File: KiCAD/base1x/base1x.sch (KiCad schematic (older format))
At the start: 83 parts, among them J1 Conn_02x05_Odd_Even, J10 Conn_01x03, J11 Conn_01x03, J12 Conn_01x03, J13 Conn_01x03, J14 Conn_01x03, J15 Conn_01x08, J17 Conn_01x03, J18 Conn_01x03, J19 Conn_01x03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

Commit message: base1x doneish
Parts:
- removed R10, R9: 50R, Resistor_SMD:R_1206_3216Metric, symbol Device:R_Small
- removed R7: 900k, Resistor_SMD:R_1206_3216Metric, symbol Device:R_Small
- removed R8: 100k, Resistor_SMD:R_1206_3216Metric, symbol Device:R_Small
- removed U6, U7: AD8615, Package_TO_SOT_SMD:TSOT-23-5, symbol Amplifier_Operational:AD8603
- added C14, C15, C16, C17, C18: 0.1uF, Capacitor_SMD:C_1206_3216Metric, symbol Device:C_Small
- added J16: Conn_02x05_Odd_Even, Connector_IDC:IDC-Header_2x05_P2.54mm_Vertical, symbol Connector_Generic:Conn_02x05_Odd_Even
- added J20: Conn_01x03, Connector_PinHeader_1.27mm:PinHeader_1x03_P1.27mm_Vertical, symbol Connector_Generic:Conn_01x03
- added JP4: Jumper_NO_Small, Jumper:SolderJumper-2_P1.3mm_Open_RoundedPad1.0x1.5mm, symbol Device:Jumper_NO_Small
- added R4: 51R, Resistor_SMD:R_1206_3216Metric_Pad1.42x1.75mm_HandSolder, symbol Device:R_Small
- added U1: AD8616, Package_SO:SOIC-8_3.9x4.9mm_P1.27mm, symbol Amplifier_Operational:AD8620
- C1, C2, C3, C5, C6, C8: farnell code (none) -> 1759297
- C10, C9: farnell code (none) -> 1759453
- C11, C4, C7: value 1000pF -> 0.1uF; farnell code 1855909 -> 1759297
- C12, C13: footprint (none) -> Capacitor_Tantalum_SMD:CP_EIA-7343-43_Kemet-X_Pad2.25x2.55mm_HandSolder
- D1, D2: I_max 20mA -> 2mA
- D10, D3, D4, D5, D6, D7, D8, D9: farnellCode (none) -> 9843760
- J1: footprint Connector_IDC:IDC-Header_2x05_P2.54mm_Horizontal -> Connector_IDC:IDC-Header_2x05_P2.54mm_Vertical; farnellCode 2215290 -> 2215304
- J10, J11, J12, J13, J14, J17, J18, J19, J2, J4, J5: footprint (none) -> Connector_PinHeader_1.27mm:PinHeader_1x03_P1.27mm_Vertical; farnell code (none) -> 2578712+2505013
- J15: footprint (none) -> Converter_DCDC:Converter_DCDC_TRACO_TMR-xxxx_THT; Farnell Code (none) -> 495-TMR6-0521
- J3: farnell code (none) -> 1097986
- J6: value Conn_02x14_Counter_Clockwise -> Conn_01x14_Counter_Clockwise; footprint Connector_PinSocket_2.54mm:PinSocket_2x14_P2.54mm_Vertical -> Connector_PinHeader_2.54mm:PinHeader_1x14_P2.54mm_Vertical; farnellCode (none) -> 1593466
- JP3: footprint (none) -> Jumper:SolderJumper-2_P1.3mm_Open_RoundedPad1.0x1.5mm
- R1: footprint Resistor_SMD:R_1206_3216Metric -> Resistor_SMD:R_2010_5025Metric_Pad1.52x2.65mm_HandSolder; farnellCode 2073607 -> 1887405
- R11: value 50R -> 51R; footprint Resistor_SMD:R_1206_3216Metric -> Resistor_SMD:R_1206_3216Metric_Pad1.42x1.75mm_HandSolder; farnellCode 2476379 -> 2695165
- R2, R3: value 100R -> 1k; footprint Resistor_SMD:R_1206_3216Metric -> Resistor_SMD:R_1206_3216Metric_Pad1.42x1.75mm_HandSolder; farnellCode 2476379 -> 2447473
- R5: value 900k -> 51R; footprint Resistor_SMD:R_1206_3216Metric -> Resistor_SMD:R_1206_3216Metric_Pad1.42x1.75mm_HandSolder; farnellCode 2476379 -> 2695165
- R6: value 100k -> 1k; footprint Resistor_SMD:R_1206_3216Metric -> Resistor_SMD:R_1206_3216Metric_Pad1.42x1.75mm_HandSolder; farnellCode 2476379 -> 2447473
- U2, U5: footprint (none) -> Package_SO:TSSOP-16_4.4x5mm_P0.65mm; Farnell Code (none) -> 296-50885-1-ND
- U8: value LT1963AxQ-2.5 -> LT1963EQ-2.5; Farnell Code (none) -> LT1963EQ-2.5#PBF-ND
- U9: value LT3015xQ-2.5 -> LT3015EQ-2.5; Farnell Code (none) -> 584-LT3015EQ-2.5#PBF
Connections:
- net +2V5: now also C4.2, C8.1, C16.1, U1.8 (V+); no longer C5.1, R5.2
- net +5V: now also C7.1, C14.1, J16.2 (Pin_2); no longer C3.1, C8.1
- net -2V5: now also C11.1, C5.2, C17.1, U1.4 (V-); no longer C6.1
- net EnableTraco: now also J16.5 (Pin_5)
- net GND: now also C7.2, C14.2, J16.6 (Pin_6); no longer C3.2, C8.2
- net GNDREF: now also C11.2, C4.1, C5.1, C8.2, C16.2, C17.2, U1.3 (+), U1.5 (+); no longer C5.2, C6.2, R6.1
- net MISO: now also J16.1 (Pin_1)
- net MOSI: now also J16.4 (Pin_4)
- net SCK: now also J16.3 (Pin_3)
- net SCL: now also J16.8 (Pin_8)
- net SDA: now also J16.7 (Pin_7)
- net V_Current: now also R11.2, U2.10 (AIN1); no longer C4.2, R1.1, R11.1, TP2.1, U3.1
- net V_D1: now also R5.2
- net V_D2: now also R4.2
- net Vin: now also JP4.1
- net ~CS0: now also J16.10 (Pin_10)
- net at D1.1 (K), R3.2: now also C18.1, U1.2 (-); no longer C11.1
- net at D2.1 (K), R2.2: now also C15.1, U1.6 (-); no longer C7.1
- net at R2.1, TP4.1: now also C15.2, R4.1, U1.7; no longer C7.2
- net at R5.1: now also R3.1, TP3.1, C18.2, U1.1; no longer R6.2
- net at J4.3 (Pin_3), R1.2, U3.4 (-): now also C3.2, C6.2, R6.1; no longer C4.1
- new net: J16.9 (Pin_9), JP4.2
- new net: J20.2 (Pin_2), R11.1, TP2.1, U3.1
- new net: C3.1, J20.1 (Pin_1), R1.1
- new net: C6.1, J20.3 (Pin_3), R6.2
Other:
- note added: "1 Sun -> ~~1mA through the PD -> ~~1V to the ADC"
- note added: "COMM_BUS_MIRROR"
- note added: "Consider switching to LT1997-1 (this TIA limits current to 150mA)"
- note added: "Gain=20V/A\nor 1000V/A\n(dark mode)"
- note removed: "Bias Voltage"
- note removed: "Current Sense TIA"
- note removed: "Gain=20V/A"
- moved on the sheet: D10, D2, D3, D4, D5, D6, D7, D8, D9, J13, J14, J17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

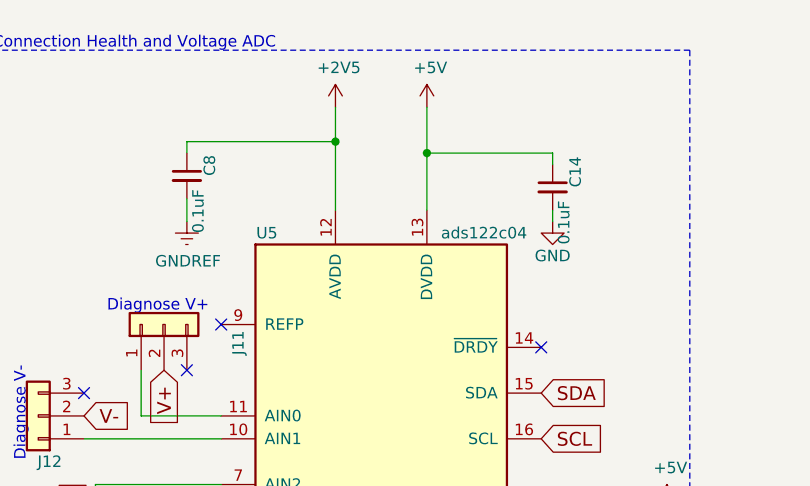
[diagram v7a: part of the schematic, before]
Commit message: new base1x layed out, mux updated and re-layed out
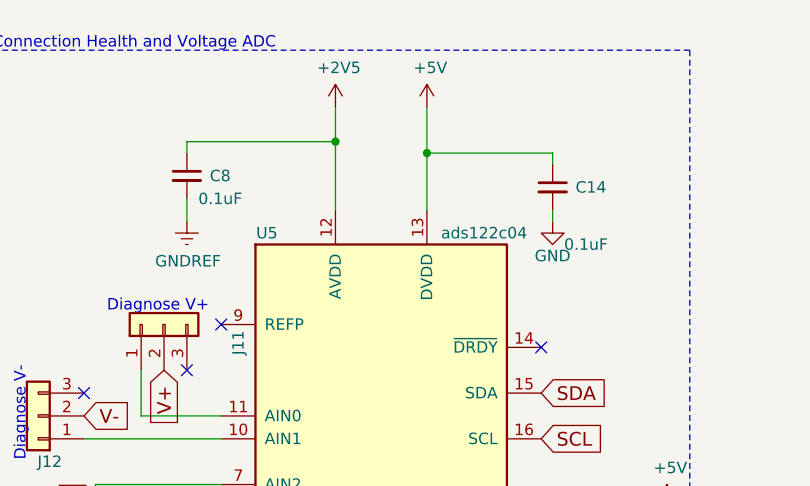
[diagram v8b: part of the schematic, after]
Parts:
- C1, C10, C11, C14, C15, C16, C17, C18, C2, C3, C4, C5, C6, C7, C8, C9: footprint Capacitor_SMD:C_1206_3216Metric -> Capacitor_SMD:C_1206_3216Metric_Pad1.42x1.75mm_HandSolder
- J6: footprint Connector_PinHeader_2.54mm:PinHeader_1x14_P2.54mm_Vertical -> Connector_PinSocket_2.54mm:PinSocket_1x14_P2.54mm_Vertical
- L1: footprint logo:logo_and_text -> logo:text
- R1: footprint Resistor_SMD:R_2010_5025Metric_Pad1.52x2.65mm_HandSolder -> Resistor_SMD:R_1206_3216Metric_Pad1.42x1.75mm_HandSolder
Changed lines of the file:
@@
 F 0 "L1" H 9050 6675 60  0001 C CNN
 F 1 "grey@mutovis.com" H 9000 6550 100 0000 C CNN
-F 2 "logo:logo_and_text" H 9050 6800 60  0001 C CNN
+F 2 "logo:text" H 9050 6800 60  0001 C CNN
 F 3 "" H 9050 6800 60  0001 C CNN
 	1    9050 6800
@@
 F 0 "J6" H 10950 6350 50  0000 C CNN
 F 1 "Conn_01x14_Counter_Clockwise" H 10950 6376 50  0001 C CNN
-F 2 "Connector_PinHeader_2.54mm:PinHeader_1x14_P2.54mm_Vertical" H 10900 5650 50  0001 C CNN
+F 2 "Connector_PinSocket_2.54mm:PinSocket_1x14_P2.54mm_Vertical" H 10900 5650 50  0001 C CNN
 F 3 "" H 10900 5650 50  0001 C CNN
 F 4 "1593466" H 0   0   50  0001 C CNN "farnellCode"
@@
 F 0 "C9" H 7292 1596 50  0000 L CNN
 F 1 "10uF" H 7292 1505 50  0000 L CNN
-F 2 "Capacitor_SMD:C_1206_3216Metric" H 7200 1550 50  0001 C CNN
+F 2 "Capacitor_SMD:C_1206_3216Metric_Pad1.42x1.75mm_HandSolder" H 7200 1550 50  0001 C CNN
 F 3 "" H 7200 1550 50  0001 C CNN
 F 4 "1759453" H 0   0   50  0001 C CNN "farnell code"
@@
 F 0 "C10" H 7292 2846 50  0000 L CNN
 F 1 "10uF" H 7292 2755 50  0000 L CNN
-F 2 "Capacitor_SMD:C_1206_3216Metric" H 7200 2800 50  0001 C CNN
+F 2 "Capacitor_SMD:C_1206_3216Metric_Pad1.42x1.75mm_HandSolder" H 7200 2800 50  0001 C CNN
 F 3 "" H 7200 2800 50  0001 C CNN
 F 4 "1759453" H 0   0   50  0001 C CNN "farnell code"
@@
 F 0 "R1" V 1950 4300 50  0000 C CNN
 F 1 "20R" V 2155 4300 50  0000 C CNN
-F 2 "Resistor_SMD:R_2010_5025Metric_Pad1.52x2.65mm_HandSolder" H 2050 4300 50  0001 C CNN
+F 2 "Resistor_SMD:R_1206_3216Metric_Pad1.42x1.75mm_HandSolder" H 2050 4300 50  0001 C CNN
 F 3 "" H 2050 4300 50  0001 C CNN
 F 4 "1887405" H -4950 1950 50  0001 C CNN "farnellCode"
@@
 F 0 "C15" V 7150 4950 50  0000 L CNN
 F 1 "0.1uF" V 7100 4700 50  0000 L CNN
-F 2 "Capacitor_SMD:C_1206_3216Metric" H 7050 4950 50  0001 C CNN
+F 2 "Capacitor_SMD:C_1206_3216Metric_Pad1.42x1.75mm_HandSolder" H 7050 4950 50  0001 C CNN
 F 3 "" H 7050 4950 50  0001 C CNN
 F 4 "1759297" V 7050 4950 50  0001 C CNN "farnell code"
@@
 F 0 "C18" V 9700 4900 50  0000 L CNN
 F 1 "0.1uF" V 9650 4650 50  0000 L CNN
-F 2 "Capacitor_SMD:C_1206_3216Metric" H 9600 4900 50  0001 C CNN
+F 2 "Capacitor_SMD:C_1206_3216Metric_Pad1.42x1.75mm_HandSolder" H 9600 4900 50  0001 C CNN
 F 3 "" H 9600 4900 50  0001 C CNN
 F 4 "1759297" V 9600 4900 50  0001 C CNN "farnell code"
@@
 F 0 "C16" V 8600 5100 50  0000 L CNN
 F 1 "0.1uF" V 8550 4850 50  0000 L CNN
-F 2 "Capacitor_SMD:C_1206_3216Metric" H 8500 5100 50  0001 C CNN
+F 2 "Capacitor_SMD:C_1206_3216Metric_Pad1.42x1.75mm_HandSolder" H 8500 5100 50  0001 C CNN
 F 3 "" H 8500 5100 50  0001 C CNN
 F 4 "1759297" V 8500 5100 50  0001 C CNN "farnell code"
@@
 F 0 "C17" V 8600 5800 50  0000 L CNN
 F 1 "0.1uF" V 8550 5550 50  0000 L CNN
-F 2 "Capacitor_SMD:C_1206_3216Metric" H 8500 5800 50  0001 C CNN
+F 2 "Capacitor_SMD:C_1206_3216Metric_Pad1.42x1.75mm_HandSolder" H 8500 5800 50  0001 C CNN
 F 3 "" H 8500 5800 50  0001 C CNN
 F 4 "1759297" V 8500 5800 50  0001 C CNN "farnell code"
@@
 F 0 "C2" V 1850 3300 50  0000 L CNN
 F 1 "0.1uF" V 1800 3050 50  0000 L CNN
-F 2 "Capacitor_SMD:C_1206_3216Metric" H 1750 3300 50  0001 C CNN
+F 2 "Capacitor_SMD:C_1206_3216Metric_Pad1.42x1.75mm_HandSolder" H 1750 3300 50  0001 C CNN
 F 3 "" H 1750 3300 50  0001 C CNN
 F 4 "1759297" V 1750 3300 50  0001 C CNN "farnell code"
@@
 F 0 "C3" V 1650 4200 50  0000 L CNN
 F 1 "0.1uF" V 1850 4200 50  0000 L CNN
-F 2 "Capacitor_SMD:C_1206_3216Metric" H 1750 4300 50  0001 C CNN
+F 2 "Capacitor_SMD:C_1206_3216Metric_Pad1.42x1.75mm_HandSolder" H 1750 4300 50  0001 C CNN
 F 3 "" H 1750 4300 50  0001 C CNN
 F 4 "1759297" V 1750 4300 50  0001 C CNN "farnell code"
@@
 F 0 "C6" V 2400 4200 50  0000 L CNN
 F 1 "0.1uF" V 2600 4200 50  0000 L CNN
-F 2 "Capacitor_SMD:C_1206_3216Metric" H 2500 4300 50  0001 C CNN
+F 2 "Capacitor_SMD:C_1206_3216Metric_Pad1.42x1.75mm_HandSolder" H 2500 4300 50  0001 C CNN
 F 3 "" H 2500 4300 50  0001 C CNN
 F 4 "1759297" V 2500 4300 50  0001 C CNN "farnell code"
@@
 F 0 "C11" V 4650 3800 50  0000 L CNN
 F 1 "0.1uF" V 4600 3550 50  0000 L CNN
-F 2 "Capacitor_SMD:C_1206_3216Metric" H 4550 3800 50  0001 C CNN
+F 2 "Capacitor_SMD:C_1206_3216Metric_Pad1.42x1.75mm_HandSolder" H 4550 3800 50  0001 C CNN
 F 3 "" H 4550 3800 50  0001 C CNN
 F 4 "1759297" V 4550 3800 50  0001 C CNN "farnell code"
@@
 U 1 1 5CAC4FC4
 P 5700 1200
-F 0 "C14" V 5800 1200 50  0000 L CNN
-F 1 "0.1uF" V 5750 950 50  0000 L CNN
-F 2 "Capacitor_SMD:C_1206_3216Metric" H 5700 1200 50  0001 C CNN
+F 0 "C14" H 5800 1200 50  0000 L CNN
+F 1 "0.1uF" H 5750 950 50  0000 L CNN
+F 2 "Capacitor_SMD:C_1206_3216Metric_Pad1.42x1.75mm_HandSolder" H 5700 1200 50  0001 C CNN
 F 3 "" H 5700 1200 50  0001 C CNN
 F 4 "1759297" V 5700 1200 50  0001 C CNN "farnell code"
@@
 U 1 1 5CAC50BC
 P 4100 1150
-F 0 "C8" V 4200 1150 50  0000 L CNN
-F 1 "0.1uF" V 4150 900 50  0000 L CNN
-F 2 "Capacitor_SMD:C_1206_3216Metric" H 4100 1150 50  0001 C CNN
+F 0 "C8" H 4200 1150 50  0000 L CNN
+F 1 "0.1uF" H 4150 1050 50  0000 L CNN
+F 2 "Capacitor_SMD:C_1206_3216Metric_Pad1.42x1.75mm_HandSolder" H 4100 1150 50  0001 C CNN
 F 3 "" H 4100 1150 50  0001 C CNN
 F 4 "1759297" V 4100 1150 50  0001 C CNN "farnell code"
@@
 F 0 "C7" V 2700 1000 50  0000 L CNN
 F 1 "0.1uF" V 2650 750 50  0000 L CNN
-F 2 "Capacitor_SMD:C_1206_3216Metric" H 2600 1000 50  0001 C CNN
+F 2 "Capacitor_SMD:C_1206_3216Metric_Pad1.42x1.75mm_HandSolder" H 2600 1000 50  0001 C CNN
 F 3 "" H 2600 1000 50  0001 C CNN
 F 4 "1759297" V 2600 1000 50  0001 C CNN "farnell code"
@@
 F 0 "C1" V 1100 900 50  0000 L CNN
 F 1 "0.1uF" V 1050 650 50  0000 L CNN
-F 2 "Capacitor_SMD:C_1206_3216Metric" H 1000 900 50  0001 C CNN
+F 2 "Capacitor_SMD:C_1206_3216Metric_Pad1.42x1.75mm_HandSolder" H 1000 900 50  0001 C CNN
 F 3 "" H 1000 900 50  0001 C CNN
 F 4 "1759297" V 1000 900 50  0001 C CNN "farnell code"
@@
 F 0 "C4" V 2000 4800 50  0000 L CNN
 F 1 "0.1uF" V 1950 4550 50  0000 L CNN
-F 2 "Capacitor_SMD:C_1206_3216Metric" H 1900 4800 50  0001 C CNN
+F 2 "Capacitor_SMD:C_1206_3216Metric_Pad1.42x1.75mm_HandSolder" H 1900 4800 50  0001 C CNN
 F 3 "" H 1900 4800 50  0001 C CNN
 F 4 "1759297" V 1900 4800 50  0001 C CNN "farnell code"
@@
 F 0 "C5" V 2000 5600 50  0000 L CNN
 F 1 "0.1uF" V 1950 5350 50  0000 L CNN
-F 2 "Capacitor_SMD:C_1206_3216Metric" H 1900 5600 50  0001 C CNN
+F 2 "Capacitor_SMD:C_1206_3216Metric_Pad1.42x1.75mm_HandSolder" H 1900 5600 50  0001 C CNN
 F 3 "" H 1900 5600 50  0001 C CNN
 F 4 "1759297" V 1900 5600 50  0001 C CNN "farnell code"
